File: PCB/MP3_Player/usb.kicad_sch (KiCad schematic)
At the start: 12 parts, among them J2 USB_C_Receptacle, J3 USB_A, U4 TS3USB30ERSWR

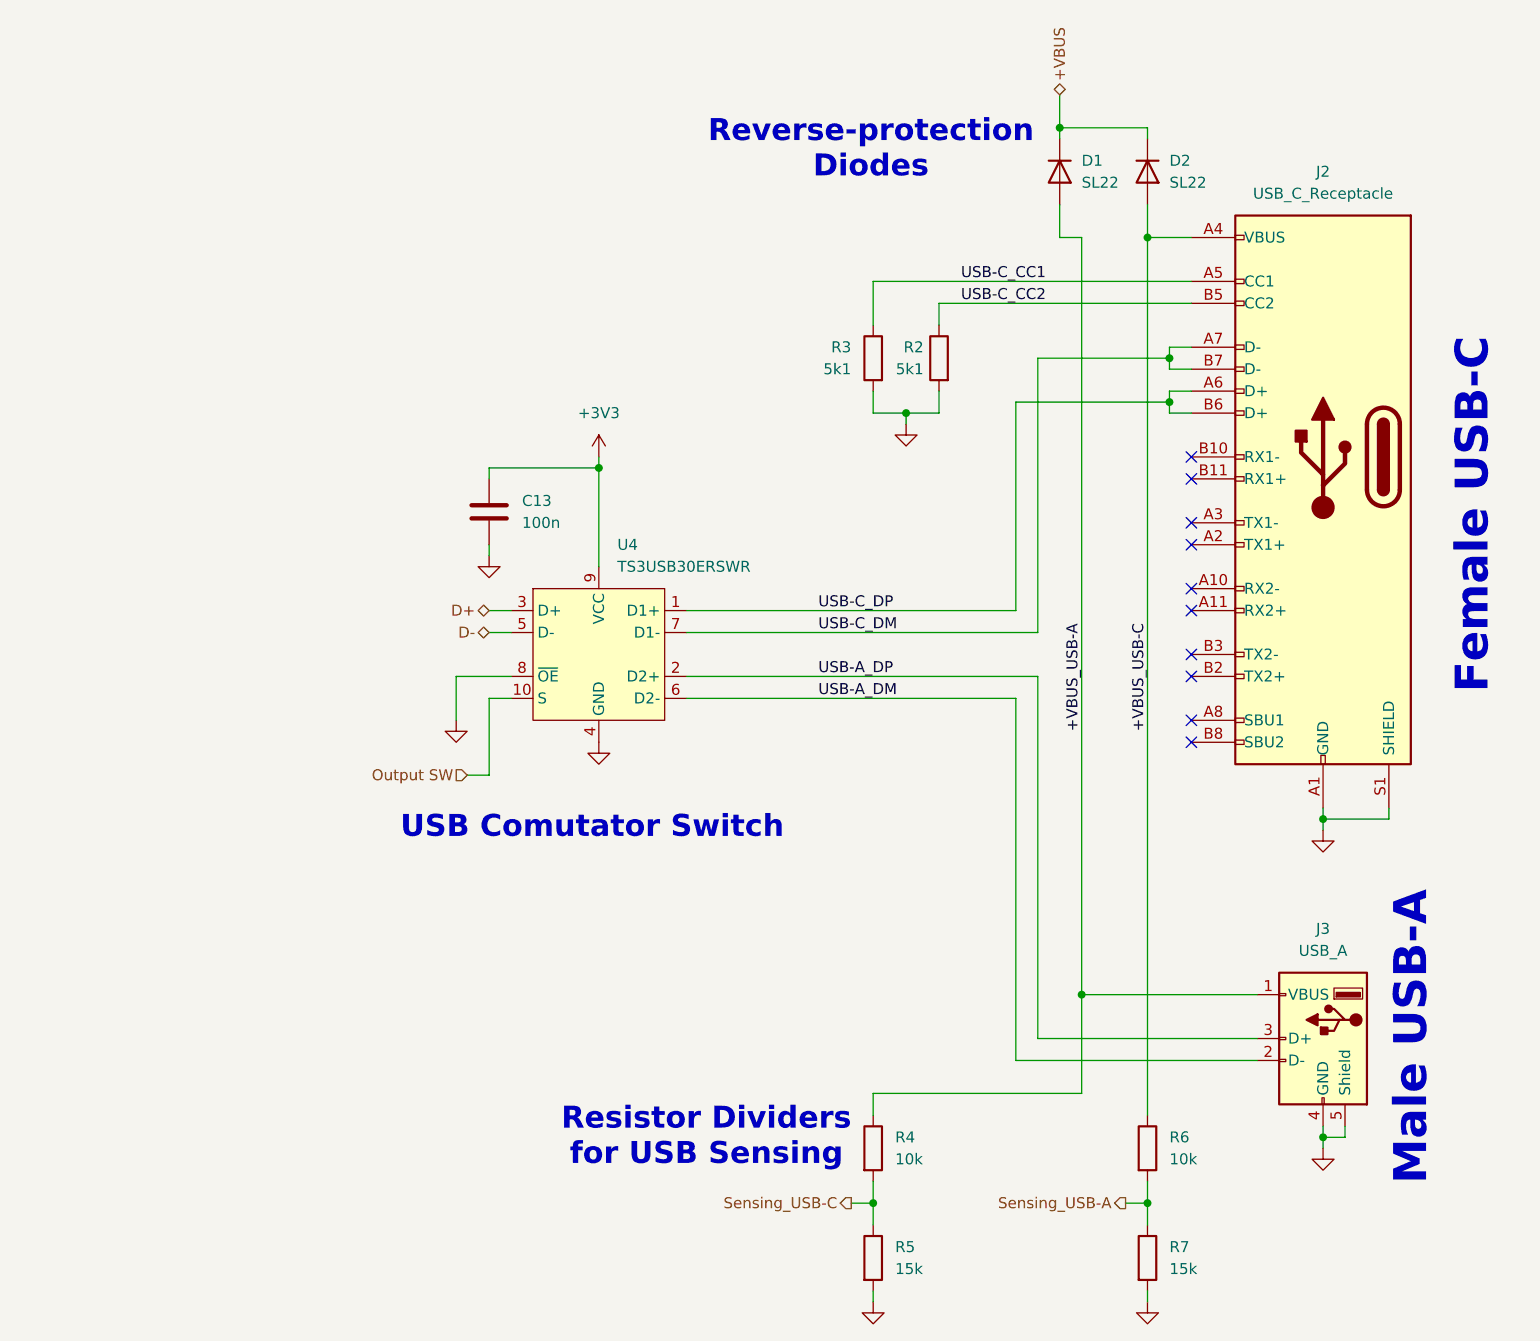
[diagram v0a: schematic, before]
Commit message: Visual Schematic Corrections
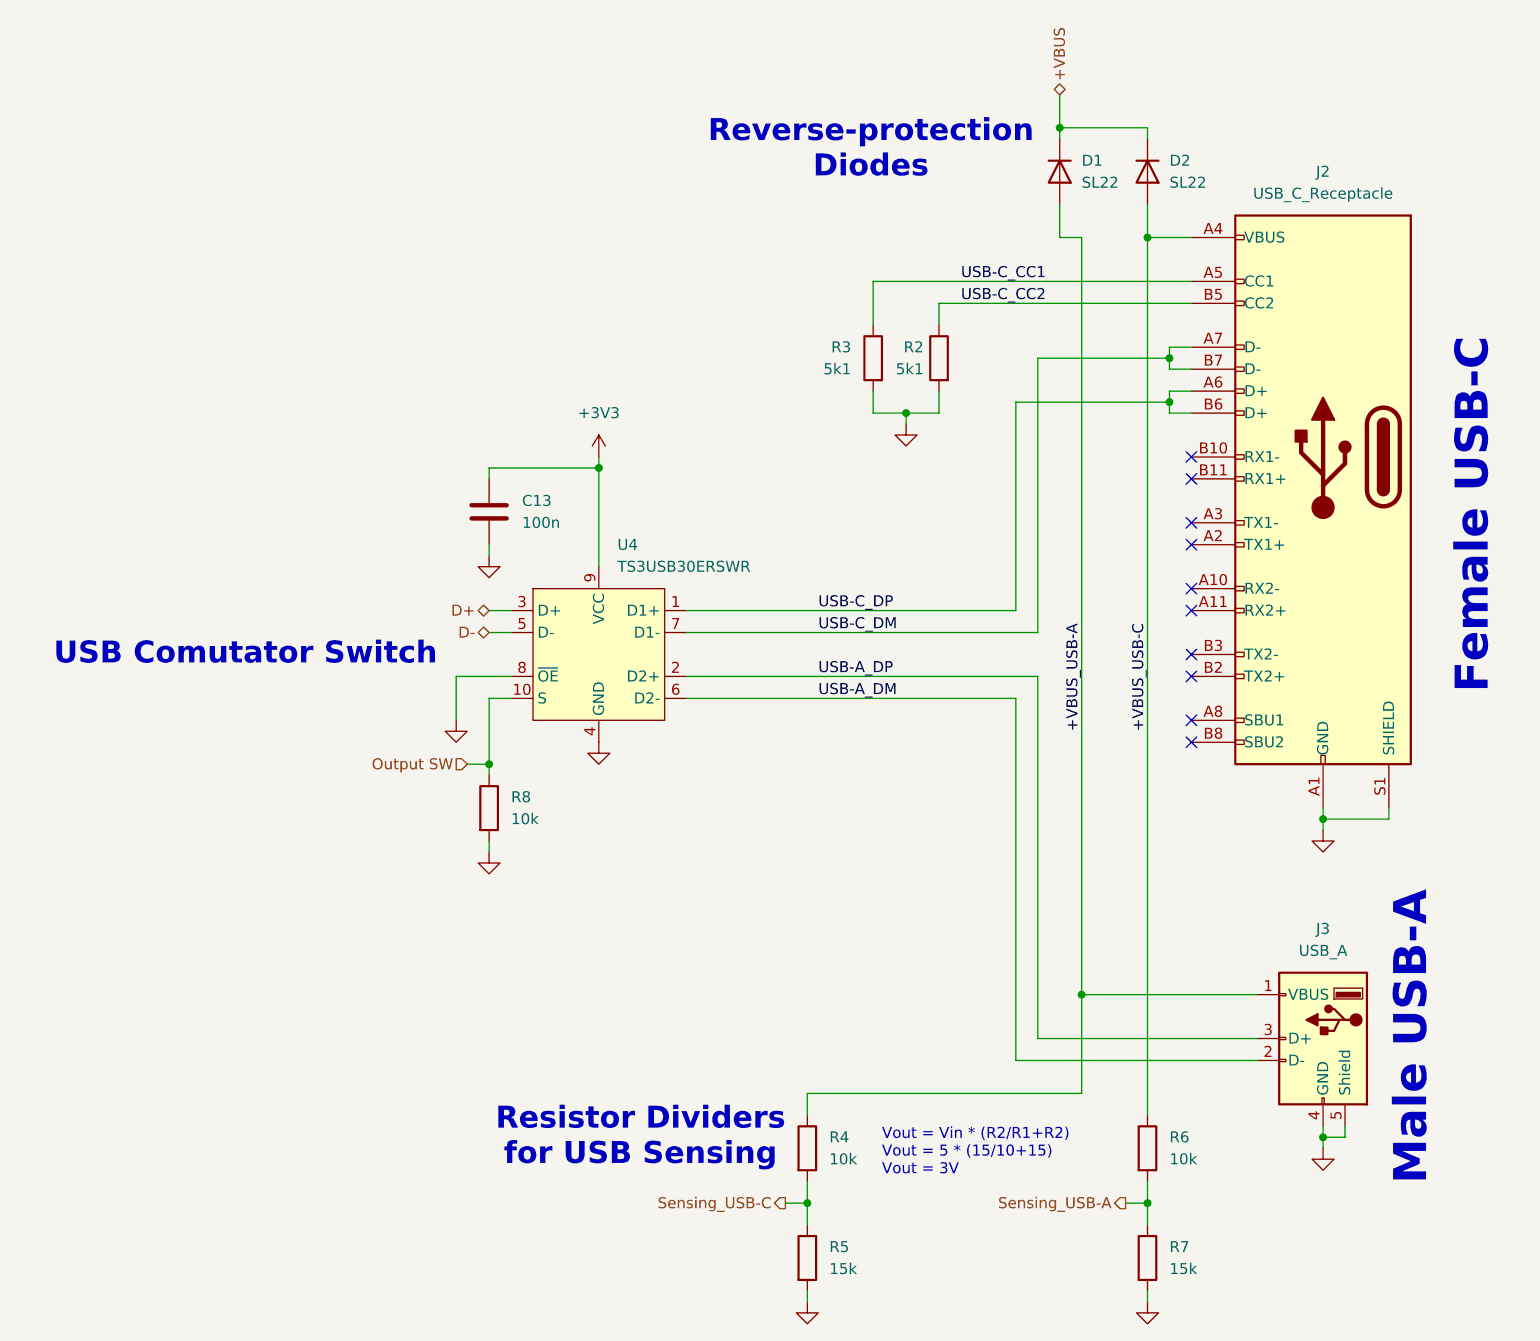
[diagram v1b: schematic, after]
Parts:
- added R8: 10k, symbol Device:R
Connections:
- net GND: now also R8.2
- net Output SW: now also R8.1
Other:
- note added: "Vout = Vin * (R2/R1+R2) Vout = 5 * (15/10+15) Vout = 3V"
- moved on the sheet: R4, R5

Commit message: Started Making BOM
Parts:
- C13: Mfr. Part # (none) -> CL05B104KP5NNNC; Store URL - Digikey (none) -> https://www.digikey.pt/pt/products/detail/samsung-electro-m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; Store URL - Mouser (none) -> https://pt.mouser.com/en/ProductDetail/Samsung-Electro-Mech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
- D1, D2: Mfr. Part # (none) -> SL22-E3/5BT; Store URL - Digikey (none) -> https://www.digikey.pt/pt/products/detail/vishay-general-se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; Store URL - Mouser (none) -> https://pt.mouser.com/en/ProductDetail/Vishay-Semiconductor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

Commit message: Continue Making BOM
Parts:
- removed J2: USB_C_Receptacle, symbol Connector:USB_C_Receptacle
- added J2: USB_C_Receptacle_16P, symbol Connector:USB_C_Receptacle_USB2.0_16P
- R2, R3: Mfr. Part # (none) -> CRCW04025K10FKED; Store URL - Digikey (none) -> https://www.digikey.pt/pt/products/detail/vishay-dale/CRCW0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; Store URL - Mouser (none) -> https://pt.mouser.com/en/ProductDetail/Vishay/CRCW04025K10F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
- R4, R6, R8: Mfr. Part # (none) -> CRCW040210K0FKED; Store URL - Digikey (none) -> https://www.digikey.pt/pt/products/detail/vishay-dale/CRCW0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; Store URL - Mouser (none) -> https://pt.mouser.com/en/ProductDetail/Vishay/CRCW040210K0F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
- R5, R7: Mfr. Part # (none) -> CRCW040215K0FKED; Store URL - Digikey (none) -> https://www.digikey.pt/pt/products/detail/vishay-dale/CRCW0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; Store URL - Mouser (none) -> https://pt.mouser.com/en/ProductDetail/Vishay/CRCW040215K0F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
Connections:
- net +VBUS_USB-C: now also J2.A4 (VBUS), J2.A9 (VBUS), J2.B4 (VBUS), J2.B9 (VBUS)
- net GND: now also J2.A1 (GND), J2.A12 (GND), J2.B1 (GND), J2.B12 (GND), J2.SH (SHIELD)
- net USB-C_CC1: now also J2.A5 (CC1)
- net USB-C_CC2: now also J2.B5 (CC2)
- net USB-C_DM: now also J2.A7 (D-), J2.B7 (D-)
- net USB-C_DP: now also J2.A6 (D+), J2.B6 (D+)
- no-connect marks 10 -> 2
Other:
- moved on the sheet: D1, R2, R3

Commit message: Finished BOM; Started Footprint assignment
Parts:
- C13, R2, R3, R4, R5, R6, R7, R8: footprint (none) -> Capacitor_SMD:C_0402_1005Metric
- J3: Mfr. Part # (none) -> 931; Store URL - Digikey (none) -> https://www.digikey.pt/pt/products/detail/keystone-electron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; Store URL - Mouser (none) -> https://pt.mouser.com/en/ProductDetail/Keystone-Electronics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
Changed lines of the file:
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@@
 			)
 		)
-		(property "Footprint" ""
+		(property "Footprint" "Capacitor_SMD:C_0402_1005Metric"
 			(at 125.222 146.05 90)
 			(hide yes)
@@
 			)
 		)
-		(property "Footprint" ""
+		(property "Footprint" "Capacitor_SMD:C_0402_1005Metric"
 			(at 125.222 158.75 90)
 			(hide yes)
@@
 			)
 		)
-		(property "Footprint" ""
+		(property "Footprint" "Capacitor_SMD:C_0402_1005Metric"
 			(at 164.592 158.75 90)
 			(hide yes)
@@
 			)
 		)
-		(property "Footprint" ""
+		(property "Footprint" "Capacitor_SMD:C_0402_1005Metric"
 			(at 88.392 106.68 90)
 			(hide yes)
@@
 			)
 		)
-		(property "Datasheet" ""
+		(property "Datasheet" "https://www.keyelco.com/userAssets/file/K75p114.pdf"
 			(at 182.88 134.62 0)
 			(hide yes)
@@
 		)
 		(property "Store URL - TME" ""
+			(at 186.69 133.35 0)
+			(hide yes)
+			(show_name no)
+			(do_not_autoplace no)
+			(effects
+				(font
+					(size 1.27 1.27)
+				)
+			)
+		)
+		(property "Mfr. Part #" "931"
+			(at 186.69 133.35 0)
+			(hide yes)
+			(show_name no)
+			(do_not_autoplace no)
+			(effects
+				(font
+					(size 1.27 1.27)
+				)
+			)
+		)
+		(property "Store URL - Digikey" "https://www.digikey.pt/pt/products/detail/keystone-electronics/931/2745644"
+			(at 186.69 133.35 0)
+			(hide yes)
+			(show_name no)
+			(do_not_autoplace no)
+			(effects
+				(font
+					(size 1.27 1.27)
+				)
+			)
+		)
+		(property "Store URL - Mouser" "https://pt.mouser.com/en/ProductDetail/Keystone-Electronics/931?qs=sZfk%252BfAlGe6kAJ2DZDSUqA%3D%3D"
 			(at 186.69 133.35 0)
 			(hide yes)
@@
 			)
 		)
-		(property "Footprint" ""
+		(property "Footprint" "Capacitor_SMD:C_0402_1005Metric"
 			(at 136.398 67.31 90)
 			(hide yes)
@@
 			)
 		)
-		(property "Footprint" ""
+		(property "Footprint" "Capacitor_SMD:C_0402_1005Metric"
 			(at 144.018 67.31 90)
 			(hide yes)
@@
 			)
 		)
-		(property "Footprint" ""
+		(property "Footprint" "Capacitor_SMD:C_0402_1005Metric"
 			(at 91.1352 76.2 0)
 			(hide yes)
@@
 			)
 		)
-		(property "Footprint" ""
+		(property "Footprint" "Capacitor_SMD:C_0402_1005Metric"
 			(at 164.592 146.05 90)
 			(hide yes)

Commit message: Footprint Assingment
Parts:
- D1, D2: footprint (none) -> Diode_SMD:D_SMB
- J2: footprint (none) -> Connector_USB:USB_C_Receptacle_G-Switch_GT-USB-7010ASV
- J3: footprint (none) -> Connector_USB:USB_A_CNCTech_1001-011-01101_Horizontal
- R2, R3, R4, R5, R6, R7, R8: footprint Capacitor_SMD:C_0402_1005Metric -> Resistor_SMD:R_0402_1005Metric
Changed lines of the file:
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@@
 			)
 		)
-		(property "Footprint" "Capacitor_SMD:C_0402_1005Metric"
+		(property "Footprint" "Resistor_SMD:R_0402_1005Metric"
 			(at 125.222 146.05 90)
 			(hide yes)
@@
 			)
 		)
-		(property "Footprint" "Capacitor_SMD:C_0402_1005Metric"
+		(property "Footprint" "Resistor_SMD:R_0402_1005Metric"
 			(at 125.222 158.75 90)
 			(hide yes)
@@
 			)
 		)
-		(property "Footprint" ""
+		(property "Footprint" "Diode_SMD:D_SMB"
 			(at 161.29 33.02 0)
 			(hide yes)
@@
 			)
 		)
-		(property "Footprint" "Capacitor_SMD:C_0402_1005Metric"
+		(property "Footprint" "Resistor_SMD:R_0402_1005Metric"
 			(at 164.592 158.75 90)
 			(hide yes)
@@
 			)
 		)
-		(property "Footprint" ""
+		(property "Footprint" "Diode_SMD:D_SMB"
 			(at 166.37 33.02 0)
 			(hide yes)
@@
 			)
 		)
-		(property "Footprint" "Capacitor_SMD:C_0402_1005Metric"
+		(property "Footprint" "Resistor_SMD:R_0402_1005Metric"
 			(at 88.392 106.68 90)
 			(hide yes)
@@
 			)
 		)
-		(property "Footprint" ""
+		(property "Footprint" "Connector_USB:USB_A_CNCTech_1001-011-01101_Horizontal"
 			(at 182.88 134.62 0)
 			(hide yes)
@@
 			)
 		)
-		(property "Footprint" ""
+		(property "Footprint" "Connector_USB:USB_C_Receptacle_G-Switch_GT-USB-7010ASV"
 			(at 182.88 68.58 0)
 			(hide yes)
@@
 			)
 		)
-		(property "Footprint" "Capacitor_SMD:C_0402_1005Metric"
+		(property "Footprint" "Resistor_SMD:R_0402_1005Metric"
 			(at 136.398 67.31 90)
 			(hide yes)
@@
 			)
 		)
-		(property "Footprint" "Capacitor_SMD:C_0402_1005Metric"
+		(property "Footprint" "Resistor_SMD:R_0402_1005Metric"
 			(at 144.018 67.31 90)
 			(hide yes)
@@
 			)
 		)
-		(property "Footprint" "Capacitor_SMD:C_0402_1005Metric"
+		(property "Footprint" "Resistor_SMD:R_0402_1005Metric"
 			(at 164.592 146.05 90)
 			(hide yes)

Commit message: Footprint Assingment Complete
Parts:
- D1, D2: value SL22 -> MBR120VLSF; footprint Diode_SMD:D_SMB -> Diode_SMD:D_SOD-123F; Mfr. Part # SL22-E3/5BT -> MBR120VLSFT3G; Store URL - Digikey https://www.digikey.pt/pt/products/detail/vishay-general-se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 -> https://www.digikey.pt/pt/products/detail/onsemi/MBR120VLSF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; Store URL - Mouser https://pt.mouser.com/en/ProductDetail/Vishay-Semiconductor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 -> https://pt.mouser.com/en/ProductDetail/onsemi/MBR120VLSFT3G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
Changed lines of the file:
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@@
 			)
 		)
-		(property "Value" "SL22"
+		(property "Value" "MBR120VLSF"
 			(at 159.512 34.29 90)
 			(show_name no)
@@
 			)
 		)
-		(property "Footprint" "Diode_SMD:D_SMB"
+		(property "Footprint" "Diode_SMD:D_SOD-123F"
 			(at 161.29 33.02 0)
 			(hide yes)
@@
 			)
 		)
-		(property "Datasheet" "https://www.vishay.com/docs/88741/sl22.pdf"
+		(property "Datasheet" "https://www.onsemi.com/pdf/datasheet/mbr120vlsft1-d.pdf"
 			(at 161.29 33.02 0)
 			(hide yes)
@@
 			)
 		)
-		(property "Description" "Diode DO-214AA (SMB)"
+		(property "Description" "DIODE SCHOTTKY 20V 1A SOD123FL"
 			(at 161.29 33.02 0)
 			(hide yes)
@@
 			)
 		)
-		(property "Mfr. Part #" "SL22-E3/5BT"
+		(property "Mfr. Part #" "MBR120VLSFT3G"
 			(at 161.29 33.02 90)
 			(hide yes)
@@
 			)
 		)
-		(property "Store URL - Digikey" "https://www.digikey.pt/pt/products/detail/vishay-general-semiconductor-diodes-division/SL22-E3-5BT/2146301"
+		(property "Store URL - Digikey" "https://www.digikey.pt/pt/products/detail/onsemi/MBR120VLSFT3G/1477157?s=N4IgTCBcDaILICEBKBGMAGAagGQMoDEAVAZgHEQBdAXyA"
 			(at 161.29 33.02 90)
 			(hide yes)
@@
 			)
 		)
-		(property "Store URL - Mouser" "https://pt.mouser.com/en/ProductDetail/Vishay-Semiconductors/SL22-E3-5BT?qs=nmw3K3MsCZYHekq5zo30%252Bg%3D%3D"
+		(property "Store URL - Mouser" "https://pt.mouser.com/en/ProductDetail/onsemi/MBR120VLSFT3G?qs=3JMERSakebrD2yr9jFliaA%3D%3D"
 			(at 161.29 33.02 90)
 			(hide yes)
@@
 			)
 		)
-		(property "Value" "SL22"
+		(property "Value" "MBR120VLSF"
 			(at 168.148 34.29 90)
 			(show_name no)
@@
 			)
 		)
-		(property "Footprint" "Diode_SMD:D_SMB"
+		(property "Footprint" "Diode_SMD:D_SOD-123F"
 			(at 166.37 33.02 0)
 			(hide yes)
@@
 			)
 		)
-		(property "Datasheet" "https://www.vishay.com/docs/88741/sl22.pdf"
+		(property "Datasheet" "https://www.onsemi.com/pdf/datasheet/mbr120vlsft1-d.pdf"
 			(at 166.37 33.02 0)
 			(hide yes)
@@
 			)
 		)
-		(property "Description" "Diode DO-214AA (SMB)"
+		(property "Description" "DIODE SCHOTTKY 20V 1A SOD123FL"
 			(at 166.37 33.02 0)
 			(hide yes)
@@
 			)
 		)
-		(property "Mfr. Part #" "SL22-E3/5BT"
+		(property "Mfr. Part #" "MBR120VLSFT3G"
 			(at 166.37 33.02 90)
 			(hide yes)
@@
 			)
 		)
-		(property "Store URL - Digikey" "https://www.digikey.pt/pt/products/detail/vishay-general-semiconductor-diodes-division/SL22-E3-5BT/2146301"
+		(property "Store URL - Digikey" "https://www.digikey.pt/pt/products/detail/onsemi/MBR120VLSFT3G/1477157?s=N4IgTCBcDaILICEBKBGMAGAagGQMoDEAVAZgHEQBdAXyA"
 			(at 166.37 33.02 90)
 			(hide yes)
@@
 			)
 		)
-		(property "Store URL - Mouser" "https://pt.mouser.com/en/ProductDetail/Vishay-Semiconductors/SL22-E3-5BT?qs=nmw3K3MsCZYHekq5zo30%252Bg%3D%3D"
+		(property "Store URL - Mouser" "https://pt.mouser.com/en/ProductDetail/onsemi/MBR120VLSFT3G?qs=3JMERSakebrD2yr9jFliaA%3D%3D"
 			(at 166.37 33.02 90)
 			(hide yes)

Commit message: PCB Layout
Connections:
- net Sensing_USB-A: now also R4.2, R5.1; no longer R6.2, R7.1
- net Sensing_USB-C: now also R6.2, R7.1; no longer R4.2, R5.1
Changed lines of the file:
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@@
 		)
 	)
-	(hierarchical_label "Sensing_USB-A"
+	(hierarchical_label "Sensing_USB-C"
 		(shape output)
 		(at 163.83 152.4 180)
@@
 		)
 	)
-	(hierarchical_label "Sensing_USB-C"
+	(hierarchical_label "Sensing_USB-A"
 		(shape output)
 		(at 124.46 152.4 180)

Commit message: PCB Layout
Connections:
- net USB-A_DM renamed USB-A_DN
- net USB-C_DM renamed USB-C_DN
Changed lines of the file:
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@@
 		)
 	)
-	(label "USB-A_DM"
+	(label "USB-A_DN"
 		(at 128.27 93.98 0)
 		(effects
@@
 		)
 	)
-	(label "USB-C_DM"
+	(label "USB-C_DN"
 		(at 128.27 86.36 0)
 		(effects
